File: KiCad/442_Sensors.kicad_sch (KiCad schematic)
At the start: 7 parts, among them U4 MS560702BA03-50, U5 LSM6DSO32TR, U6 SAM-M8Q

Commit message: All footprints placed
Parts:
- U4: footprint MS560702BA03-50:SON125P300X500X100-8N -> MS56:SON8_MS5611_TEC
- U5: footprint LSM6DSO32TR:XDCR_LSM6DSO32TR -> Package_LGA:LGA-14_3x2.5mm_P0.5mm_LayoutBorder3x4y
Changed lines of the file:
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@@
 			)
 		)
-		(property "Footprint" "LSM6DSO32TR:XDCR_LSM6DSO32TR"
-			(at 107.95 57.15 0)
-			(effects
-				(font
-					(size 1.27 1.27)
+		(property "Footprint" "Package_LGA:LGA-14_3x2.5mm_P0.5mm_LayoutBorder3x4y"
+			(at 107.95 57.15 0)
+			(effects
+				(font
+					(size 1.27 1.27)
+					(italic yes)
 				)
 				(justify bottom)
@@
 			)
 		)
-		(property "Footprint" "MS560702BA03-50:SON125P300X500X100-8N"
+		(property "Footprint" "MS56:SON8_MS5611_TEC"
 			(at 106.68 101.6 0)
 			(effects

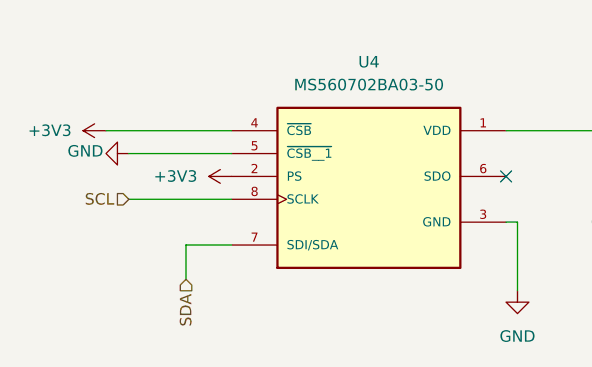
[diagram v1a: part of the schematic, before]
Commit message: I2C connections
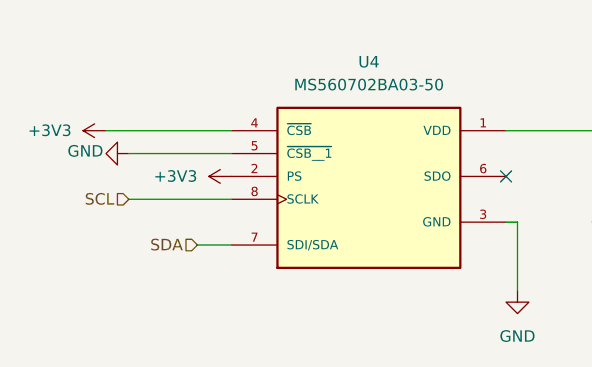
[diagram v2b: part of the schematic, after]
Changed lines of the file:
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@@
-	(wire
-		(pts
-			(xy 86.36 109.22) (xy 86.36 113.03)
-		)
-		(stroke
-			(width 0)
-			(type default)
-		)
-	)
 	(wire
 		(pts
@@
 	(wire
 		(pts
-			(xy 91.44 109.22) (xy 86.36 109.22)
+			(xy 91.44 109.22) (xy 87.63 109.22)
 		)
 		(stroke
@@
 	(hierarchical_label "SDA"
 		(shape input)
-		(at 86.36 113.03 270)
+		(at 87.63 109.22 180)
 		(effects
 			(font

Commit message: Layout updated. Very little left to do.
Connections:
- net VDD is gone; now on net +3V3: U5.12 (CS)
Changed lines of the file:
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@@
+	)
+	(junction
+		(at 142.24 46.99)
+		(diameter 0)
+		(color 0 0 0 0)
 	)
 	(junction
@@
 	)
 	(junction
-		(at 142.24 41.91)
+		(at 130.81 72.39)
 		(diameter 0)
 		(color 0 0 0 0)
 	)
 	(junction
-		(at 130.81 72.39)
+		(at 142.24 41.91)
 		(diameter 0)
 		(color 0 0 0 0)
@@
 		(color 0 0 0 0)
 	)
-	(junction
-		(at 142.24 46.99)
-		(diameter 0)
-		(color 0 0 0 0)
-	)
 	(no_connect
 		(at 168.91 76.2)
@@
 	(wire
 		(pts
-			(xy 125.73 41.91) (xy 142.24 41.91)
+			(xy 125.73 41.91) (xy 125.73 44.45)
 		)
 		(stroke
@@
 	(wire
 		(pts
-			(xy 125.73 41.91) (xy 125.73 44.45)
-		)
-		(stroke
-			(width 0)
-			(type default)
-		)
-	)
-	(wire
-		(pts
 			(xy 90.17 57.15) (xy 78.74 57.15)
 		)
@@
 	(wire
 		(pts
+			(xy 142.24 41.91) (xy 125.73 41.91)
+		)
+		(stroke
+			(width 0)
+			(type default)
+		)
+	)
+	(wire
+		(pts
 			(xy 125.73 62.23) (xy 147.32 62.23)
 		)
@@
 	(wire
 		(pts
+			(xy 168.91 59.69) (xy 171.45 59.69)
+		)
+		(stroke
+			(width 0)
+			(type default)
+		)
+	)
+	(wire
+		(pts
+			(xy 130.81 72.39) (xy 125.73 72.39)
+		)
+		(stroke
+			(width 0)
+			(type default)
+		)
+	)
+	(wire
+		(pts
+			(xy 181.61 63.5) (xy 181.61 59.69)
+		)
+		(stroke
+			(width 0)
+			(type default)
+		)
+	)
+	(wire
+		(pts
+			(xy 147.32 62.23) (xy 147.32 63.5)
+		)
+		(stroke
+			(width 0)
+			(type default)
+		)
+	)
+	(wire
+		(pts
+			(xy 142.24 41.91) (xy 142.24 39.37)
+		)
+		(stroke
+			(width 0)
+			(type default)
+		)
+	)
+	(wire
+		(pts
+			(xy 142.24 46.99) (xy 154.94 46.99)
+		)
+		(stroke
+			(width 0)
+			(type default)
+		)
+	)
+	(wire
+		(pts
 			(xy 125.73 46.99) (xy 142.24 46.99)
-		)
-		(stroke
-			(width 0)
-			(type default)
-		)
-	)
-	(wire
-		(pts
-			(xy 168.91 59.69) (xy 171.45 59.69)
-		)
-		(stroke
-			(width 0)
-			(type default)
-		)
-	)
-	(wire
-		(pts
-			(xy 130.81 72.39) (xy 125.73 72.39)
-		)
-		(stroke
-			(width 0)
-			(type default)
-		)
-	)
-	(wire
-		(pts
-			(xy 181.61 63.5) (xy 181.61 59.69)
-		)
-		(stroke
-			(width 0)
-			(type default)
-		)
-	)
-	(wire
-		(pts
-			(xy 147.32 62.23) (xy 147.32 63.5)
-		)
-		(stroke
-			(width 0)
-			(type default)
-		)
-	)
-	(wire
-		(pts
-			(xy 142.24 41.91) (xy 142.24 39.37)
-		)
-		(stroke
-			(width 0)
-			(type default)
-		)
-	)
-	(wire
-		(pts
-			(xy 142.24 46.99) (xy 154.94 46.99)
 		)
 		(stroke
@@
 	(symbol
 		(lib_id "power:+3V3")
+		(at 132.08 64.77 270)
+		(unit 1)
+		(exclude_from_sim no)
+		(in_bom yes)
+		(on_board yes)
+		(dnp no)
+		(fields_autoplaced yes)
+		(property "Reference" "#PWR078"
+			(at 128.27 64.77 0)
+			(effects
+				(font
+					(size 1.27 1.27)
+				)
+				(hide yes)
+			)
+		)
+		(property "Value" "+3V3"
+			(at 135.89 64.7699 90)
+			(effects
+				(font
+					(size 1.27 1.27)
+				)
+				(justify left)
+			)
+		)
+		(property "Footprint" ""
+			(at 132.08 64.77 0)
+			(effects
+				(font
+					(size 1.27 1.27)
+				)
+				(hide yes)
+			)
+		)
+		(property "Datasheet" ""
+			(at 132.08 64.77 0)
+			(effects
+				(font
+					(size 1.27 1.27)
+				)
+				(hide yes)
+			)
+		)
+		(property "Description" "Power symbol creates a global label with name \"+3V3\""
+			(at 132.08 64.77 0)
+			(effects
+				(font
+					(size 1.27 1.27)
+				)
+				(hide yes)
+			)
+		)
+		(pin "1"
+		)
+		(instances
+			(project "Senior Project"
+				(path "/16f8cce7-467e-4342-b55a-00af81cd6f69/c3ab4c5a-4cab-469f-8c3a-b4c939a78ff3"
+					(reference "#PWR078")
+					(unit 1)
+				)
+			)
+		)
+	)
+	(symbol
+		(lib_id "power:+3V3")
 		(at 179.07 58.42 0)
 		(unit 1)
@@
 					(unit 1)
 				)
-			)
-		)
-	)
-	(symbol
-		(lib_id "power:VDD")
-		(at 132.08 64.77 270)
-		(unit 1)
-		(exclude_from_sim no)
-		(in_bom yes)
-		(on_board yes)
-		(dnp no)
-		(fields_autoplaced yes)
-		(property "Reference" "#PWR050"
-			(at 128.27 64.77 0)
-			(effects
-				(font
-					(size 1.27 1.27)
-				)
-				(hide yes)
-			)
-		)
-		(property "Value" "VDD"
-			(at 135.89 64.7699 90)
-			(effects
-				(font
-					(size 1.27 1.27)
-				)
-				(justify left)
-			)
-		)
-		(property "Footprint" ""
-			(at 132.08 64.77 0)
-			(effects
-				(font
-					(size 1.27 1.27)
-				)
-				(hide yes)
-			)
-		)
-		(property "Datasheet" ""
-			(at 132.08 64.77 0)
-			(effects
-				(font
-					(size 1.27 1.27)
-				)
-				(hide yes)
-			)
-		)
-		(property "Description" "Power symbol creates a global label with name \"VDD\""
-			(at 132.08 64.77 0)
-			(effects
-				(font
-					(size 1.27 1.27)
-				)
-				(hide yes)
-			)
-		)
-		(pin "1"
-		)
-		(instances
-			(project "442_Sensors"
-				(path "/16f8cce7-467e-4342-b55a-00af81cd6f69/c3ab4c5a-4cab-469f-8c3a-b4c939a78ff3"
-					(reference "#PWR050")
-					(unit 1)
-				)
-			)
-			(project "442_Sensors"
-				(path "/d194a77b-7750-400f-95b2-93ee3282d6b3"
-					(reference "#PWR015")
-					(unit 1)
-				)

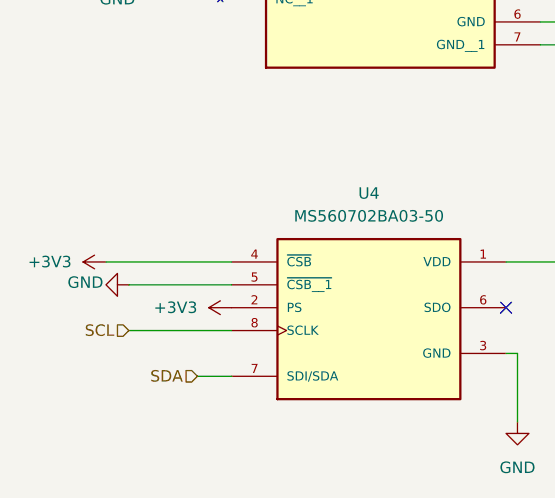
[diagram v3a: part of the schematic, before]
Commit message: Barometer schematic fix, JST connector, and few other fixes
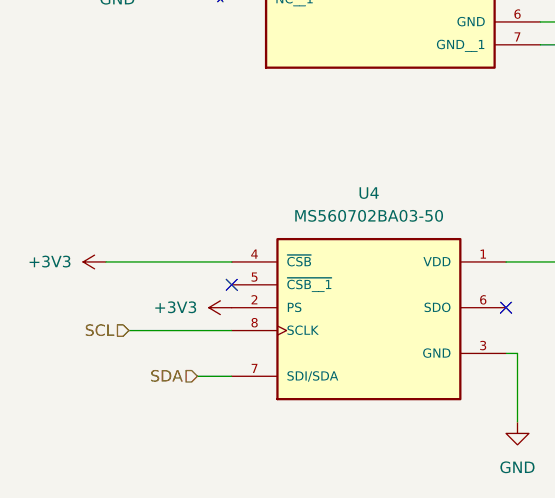
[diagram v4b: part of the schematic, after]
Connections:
- net GND: no longer U4.5 (~{CSB__1})
- no-connect marks 9 -> 10
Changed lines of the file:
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@@
+	)
+	(no_connect
+		(at 91.44 99.06)
 	)
 	(no_connect
@@
 		(pts
 			(xy 130.81 76.2) (xy 130.81 72.39)
-		)
-		(stroke
-			(width 0)
-			(type default)
-		)
-	)
-	(wire
-		(pts
-			(xy 80.01 99.06) (xy 91.44 99.06)
 		)
 		(stroke
@@
 					(unit 1)
 				)
-			)
-		)
-	)
-	(symbol
-		(lib_id "power:GND")
-		(at 80.01 99.06 270)
-		(unit 1)
-		(exclude_from_sim no)
-		(in_bom yes)
-		(on_board yes)
-		(dnp no)
-		(property "Reference" "#PWR046"
-			(at 73.66 99.06 0)
-			(effects
-				(font
-					(size 1.27 1.27)
-				)
-				(hide yes)
-			)
-		)
-		(property "Value" "GND"
-			(at 75.184 98.806 90)
-			(effects
-				(font
-					(size 1.27 1.27)
-				)
-			)
-		)
-		(property "Footprint" ""
-			(at 80.01 99.06 0)
-			(effects
-				(font
-					(size 1.27 1.27)
-				)
-				(hide yes)
-			)
-		)
-		(property "Datasheet" ""
-			(at 80.01 99.06 0)
-			(effects
-				(font
-					(size 1.27 1.27)
-				)
-				(hide yes)
-			)
-		)
-		(property "Description" "Power symbol creates a global label with name \"GND\" , ground"
-			(at 80.01 99.06 0)
-			(effects
-				(font
-					(size 1.27 1.27)
-				)
-				(hide yes)
-			)
-		)
-		(pin "1"
-		)
-		(instances
-			(project "442_Sensors"
-				(path "/16f8cce7-467e-4342-b55a-00af81cd6f69/c3ab4c5a-4cab-469f-8c3a-b4c939a78ff3"
-					(reference "#PWR046")
-					(unit 1)
-				)
-			)
-			(project "442_Sensors"
-				(path "/d194a77b-7750-400f-95b2-93ee3282d6b3"
-					(reference "#PWR06")
-					(unit 1)
-				)

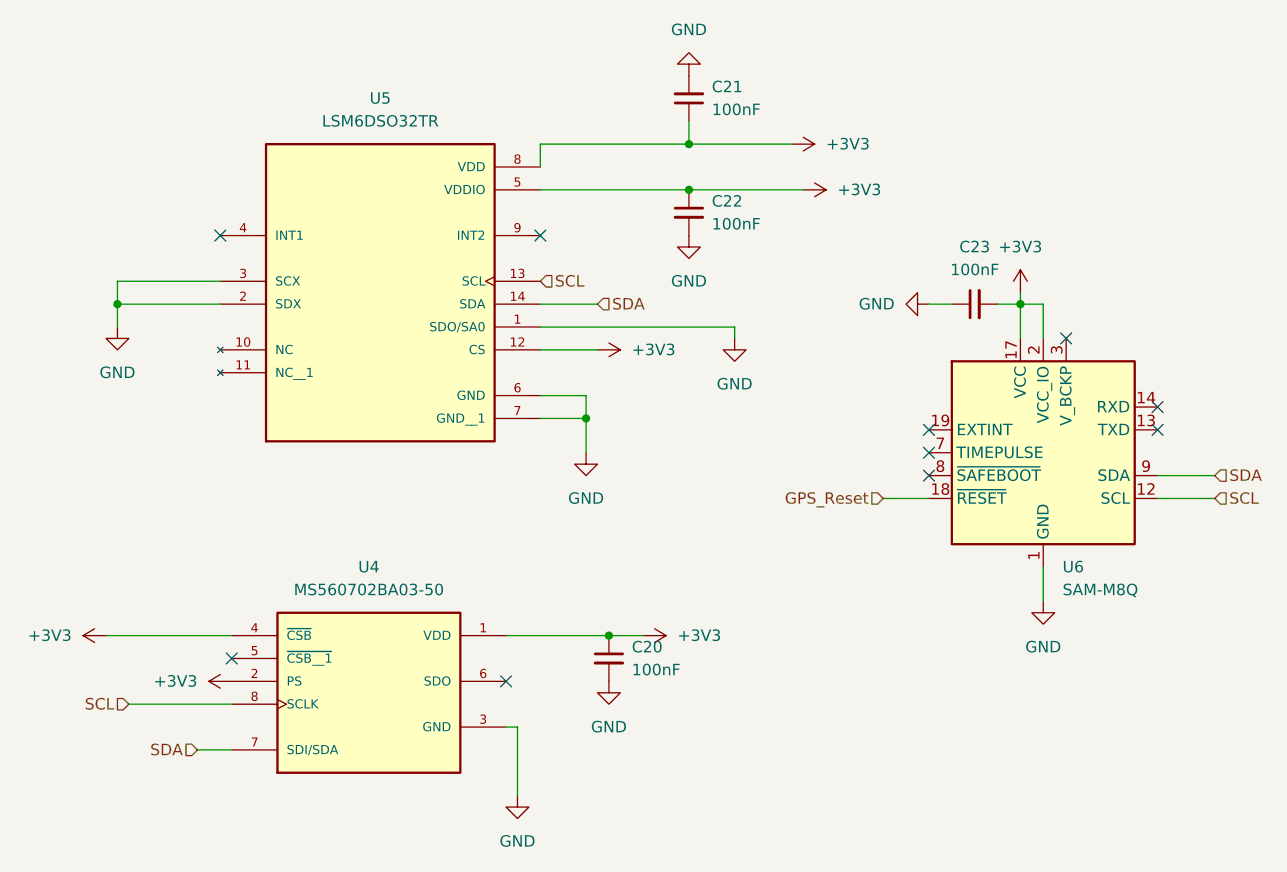
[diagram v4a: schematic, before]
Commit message: Switch added, LCSC table, other changes.
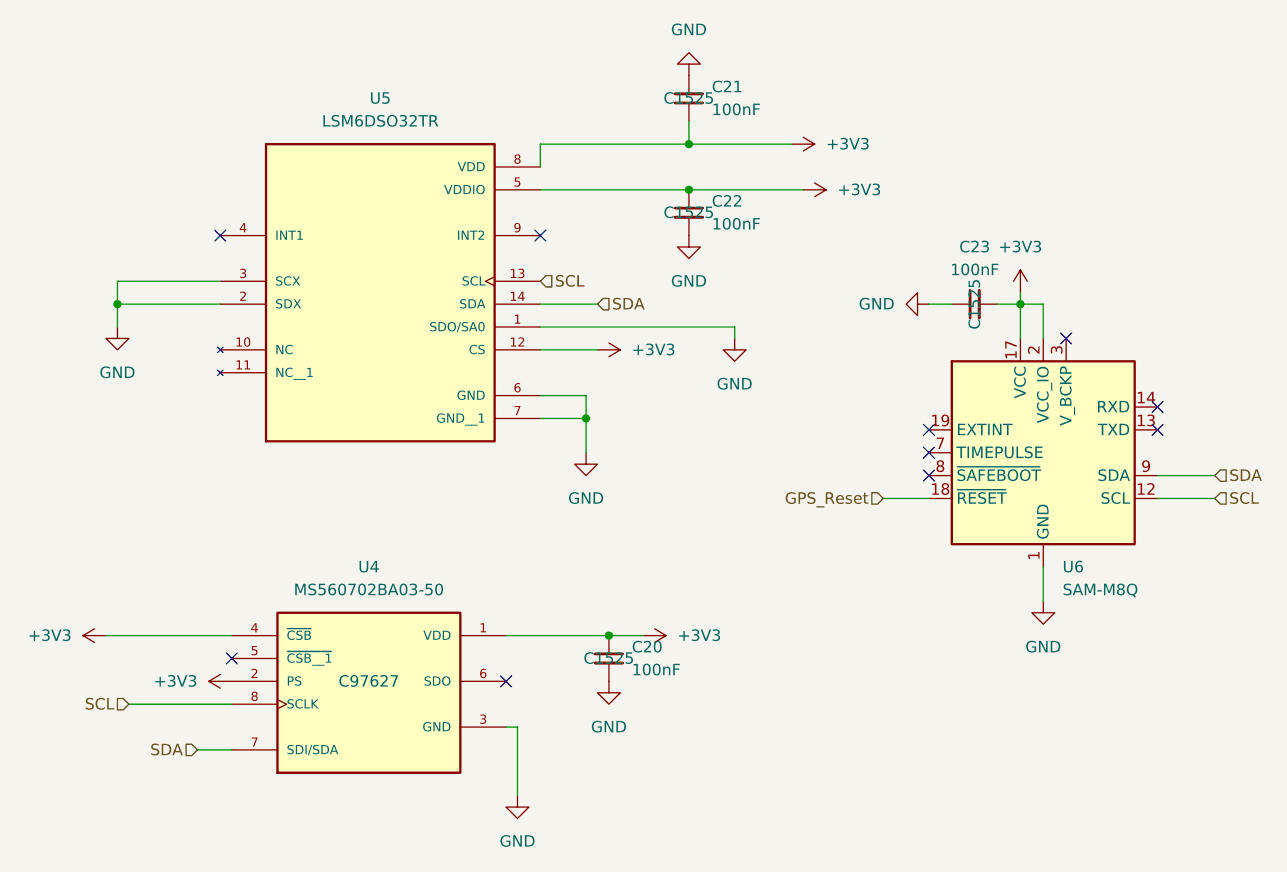
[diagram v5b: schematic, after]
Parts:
- C20, C21, C22, C23: LCSC (none) -> C1525
- U4: LCSC (none) -> C97627
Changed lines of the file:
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@@
+			)
+		)
+		(property "LCSC" "C1525"
+			(at 142.24 36.83 0)
+			(effects
+				(font
+					(size 1.27 1.27)
+				)
 			)
 		)
@@
 			)
 		)
+		(property "LCSC" ""
+			(at 107.95 57.15 0)
+			(effects
+				(font
+					(size 1.27 1.27)
+				)
+			)
+		)
 		(pin "14"
 		)
@@
 			)
 		)
+		(property "LCSC" "C97627"
+			(at 106.68 101.6 0)
+			(effects
+				(font
+					(size 1.27 1.27)
+				)
+			)
+		)
 		(pin "2"
 		)
@@
 			)
 		)
+		(property "LCSC" ""
+			(at 181.61 76.2 0)
+			(effects
+				(font
+					(size 1.27 1.27)
+				)
+			)
+		)
 		(pin "19"
 		)
@@
 			)
 		)
+		(property "LCSC" "C1525"
+			(at 133.35 99.06 0)
+			(effects
+				(font
+					(size 1.27 1.27)
+				)
+			)
+		)
 		(pin "1"
 		)
@@
 			)
 		)
+		(property "LCSC" "C1525"
+			(at 173.99 59.69 0)
+			(effects
+				(font
+					(size 1.27 1.27)
+				)
+			)
+		)
 		(pin "1"
 		)
@@
 			)
 		)
+		(property "LCSC" "C1525"
+			(at 142.24 49.53 0)
+			(effects
+				(font
+					(size 1.27 1.27)
+				)
+			)
+		)
